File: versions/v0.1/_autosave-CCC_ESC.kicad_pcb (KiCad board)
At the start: 4 copper layers, 100 x 65 mm, 155 parts, among them J1 Conn_01x04, J2 Conn_01x04, J3 Conn_01x06, J4 Conn_01x06, U1 NCP5183, U2 NCP5183, U3 NCP5183, U4 NCS20074D, U5 STM32F401CCU6_Balckpill, U6 PQDE6W-Q110, U7 TO220_replacement_module

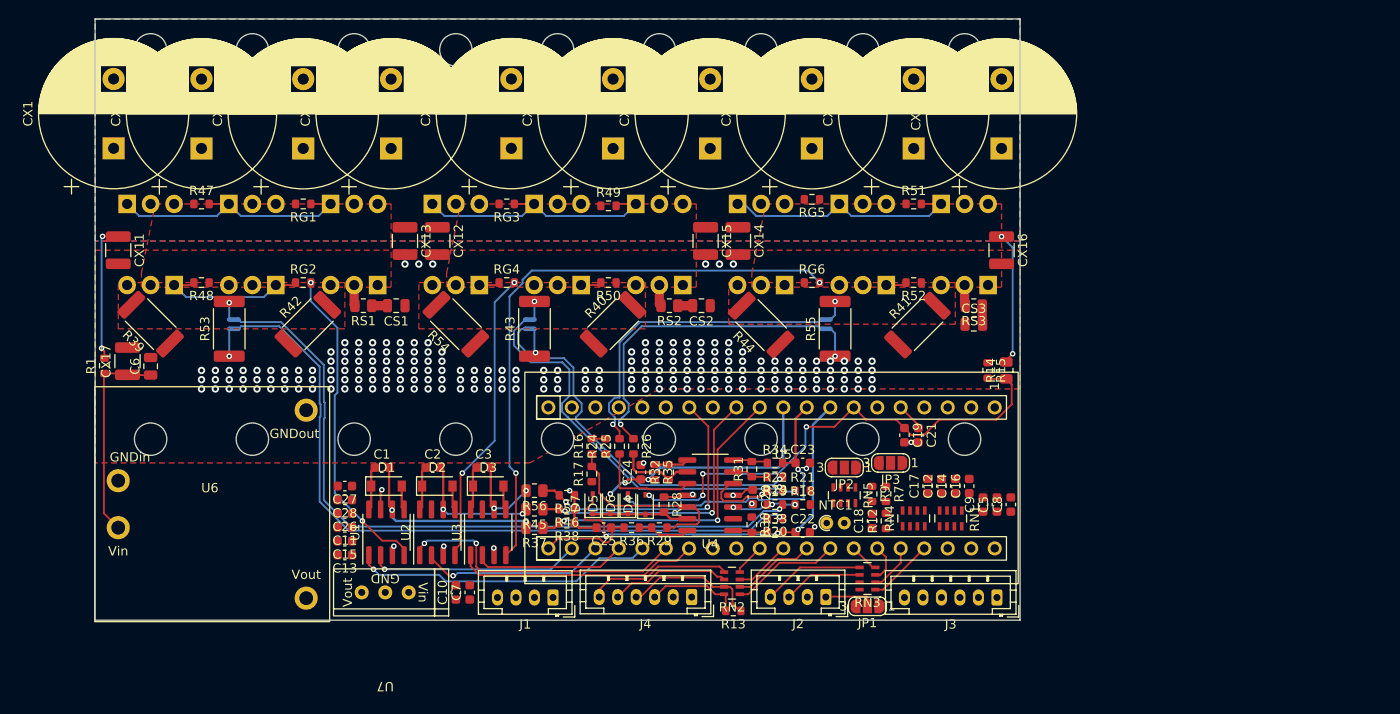
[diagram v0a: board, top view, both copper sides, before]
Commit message: work in progress - added some values and part numbers
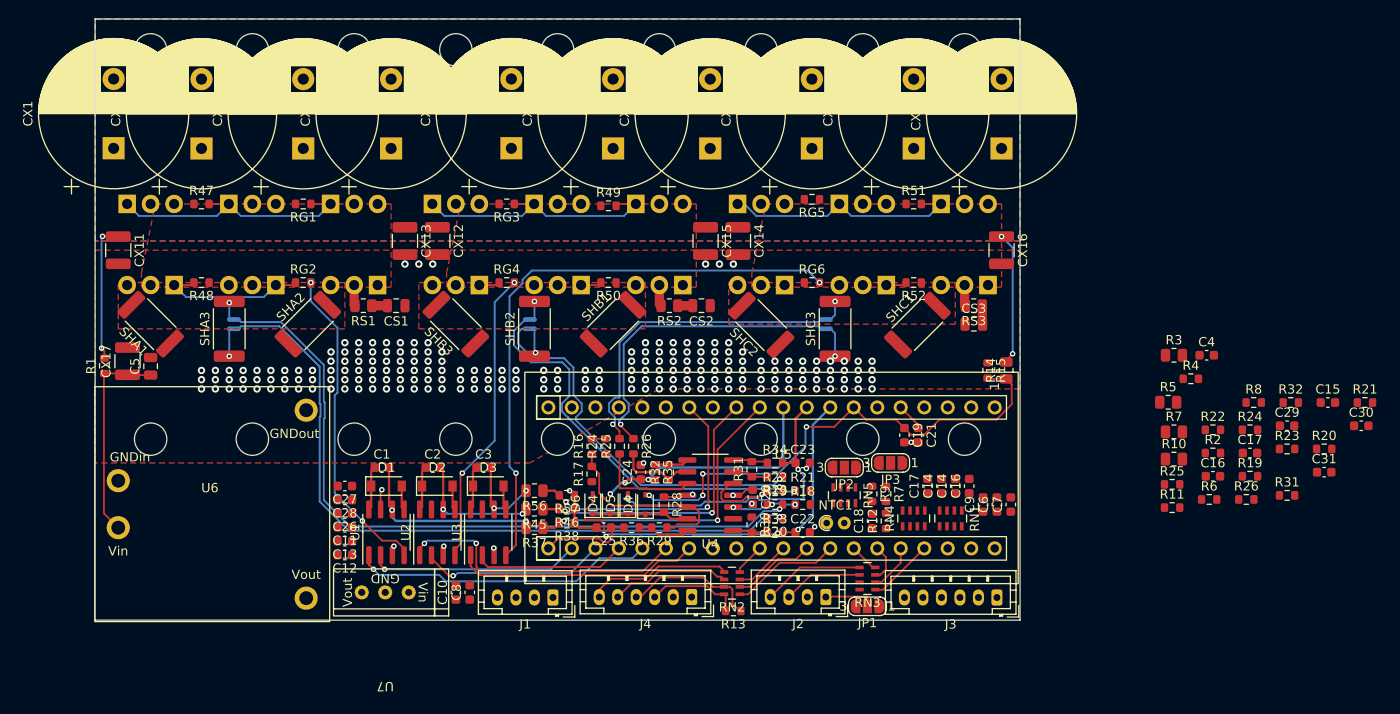
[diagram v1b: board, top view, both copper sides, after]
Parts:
- added C15: 1n5, Capacitor_SMD:C_0603_1608Metric, F.Cu at (183.3, 91.5)
- added C16: 1n5, Capacitor_SMD:C_0603_1608Metric, F.Cu at (170.8, 99.4)
- added C17: 1n5, Capacitor_SMD:C_0603_1608Metric, F.Cu at (174.9, 96.9)
- added C29: 47pF, Capacitor_SMD:C_0603_1608Metric, F.Cu at (178.9, 94.0)
- added C30: 47pF, Capacitor_SMD:C_0603_1608Metric, F.Cu at (186.9, 94.0)
- added C31: 47pF, Capacitor_SMD:C_0603_1608Metric, F.Cu at (182.9, 99.0)
- added C4: 1nF, Capacitor_SMD:C_0603_1608Metric, F.Cu at (170.2, 86.4)
- added R10: 100k, Resistor_SMD:R_0805_2012Metric, F.Cu at (166.6, 97.6)
- added R11: 3k3, Resistor_SMD:R_0603_1608Metric, F.Cu at (166.4, 102.8)
- added R19: 2k2, Resistor_SMD:R_0603_1608Metric, F.Cu at (174.9, 99.4)
- added R2: 2k2, Resistor_SMD:R_0603_1608Metric, F.Cu at (170.8, 96.9)
- added R20: 2k2, Resistor_SMD:R_0603_1608Metric, F.Cu at (182.9, 96.5)
- added R21: 47k, Resistor_SMD:R_0603_1608Metric, F.Cu at (187.3, 91.5)
- added R22: 2k2, Resistor_SMD:R_0603_1608Metric, F.Cu at (170.8, 94.4)
- added R23: 2k2, Resistor_SMD:R_0603_1608Metric, F.Cu at (178.9, 96.5)
- added R24: 47k, Resistor_SMD:R_0603_1608Metric, F.Cu at (174.9, 94.4)
- added R25: 2k2, Resistor_SMD:R_0603_1608Metric, F.Cu at (166.4, 100.3)
- added R26: 2k2, Resistor_SMD:R_0603_1608Metric, F.Cu at (174.5, 102.0)
- added R3: 1M, Resistor_SMD:R_0805_2012Metric, F.Cu at (166.6, 86.4)
- added R31: 22k, Resistor_SMD:R_0603_1608Metric, F.Cu at (178.9, 101.5)
- added R32: 22k, Resistor_SMD:R_0603_1608Metric, F.Cu at (179.3, 91.5)
- added R4: 33k, Resistor_SMD:R_0603_1608Metric, F.Cu at (168.5, 88.9)
- added R5: 100k, Resistor_SMD:R_0805_2012Metric, F.Cu at (166.0, 91.4)
- added R6: 3k3, Resistor_SMD:R_0603_1608Metric, F.Cu at (170.4, 102.0)
- added R7: 100k, Resistor_SMD:R_0805_2012Metric, F.Cu at (166.6, 94.6)
- added R8: 3k3, Resistor_SMD:R_0603_1608Metric, F.Cu at (175.3, 91.5)
- C14: renamed from C12; value 100n -> 1n5
- CX11, CX12, CX13, CX14, CX15, CX16: value 47uF -> 4.7uF
- R14: value R -> 1M
- R15: value R -> 33k
- R18: value R -> 47k
- R30: value R -> 22k
- RN1, RN4: value R_Pack04 -> 10k
- RN2, RN3: value R_Pack04 -> 100R
- RN5: value R_Pack04 -> 620R
- SHA1: renamed from R39; value R -> 1mR
- SHA2: renamed from R42; value R -> 1mR
- SHA3: renamed from R53; value R -> 1mR
- SHB1: renamed from R40; value R -> 1mR
- SHB2: renamed from R43; value R -> 1mR
- SHB3: renamed from R54; value R -> 1mR
- SHC1: renamed from R41; value R -> 1mR
- SHC2: renamed from R44; value R -> 1mR
- SHC3: renamed from R55; value R -> 1mR
- renumbered C13 to C12, C15 to C13, C6 to C5, C5 to C6, C8 to C7, C7 to C8, D5 to D4, D6 to D5, D7 to D6
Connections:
- C18 pad 1: FET_TEMP -> Net-(C18-Pad1)
- D4 pad 1: Net-(U4-Pad13) -> VSENSE2
- D5 pad 1: Net-(U4-Pad13) -> VSENSE2
- D6 pad 1: Net-(U4-Pad13) -> VSENSE2
- JP3 pad 3: Net-(U5-Pad15) -> Net-(C18-Pad1)
- R18 pad 1: Net-(U4-Pad3) -> Net-(R18-Pad1)
- R28 pad 2: Net-(U4-Pad13) -> VSENSE2
- R30 pad 1: Net-(U4-Pad2) -> Net-(R20-Pad1)
- R34 pad 1: Net-(U4-Pad7) -> Net-(R31-Pad2)
- R35 pad 1: Net-(U4-Pad8) -> Net-(R32-Pad2)
- R9 pad 1: Net-(R9-Pad1) -> GND
- R9 pad 2: GND -> Net-(R9-Pad2)
- RN5 pad 2: A_THROTTLE -> Net-(J1-Pad3)
- RN5 pad 3: Net-(J1-Pad3) -> A_THROTTLE
- RN5 pad 5: Net-(R9-Pad1) -> Net-(R9-Pad2)
- RN5 pad 6: Net-(R9-Pad1) -> Net-(RN5-Pad6)
- RN5 pad 7: Net-(R7-Pad1) -> Net-(R9-Pad2)
- RN5 pad 8: Net-(R7-Pad1) -> Net-(RN5-Pad6)
- U4 pad 10: Net-(U4-Pad10) -> Net-(R24-Pad1)
- U4 pad 13: Net-(U4-Pad13) -> VSENSE2
- U4 pad 2: Net-(U4-Pad2) -> Net-(R20-Pad1)
- U4 pad 3: Net-(U4-Pad3) -> Net-(R18-Pad1)
- U4 pad 5: Net-(U4-Pad5) -> Net-(R21-Pad1)
- U4 pad 6: Net-(U4-Pad6) -> Net-(R23-Pad1)
- U4 pad 7: Net-(U4-Pad7) -> Net-(R31-Pad2)
- U4 pad 8: Net-(U4-Pad8) -> Net-(R32-Pad2)
- U4 pad 9: Net-(U4-Pad9) -> Net-(R26-Pad1)
- U5 pad 15: Net-(U5-Pad15) -> Net-(C18-Pad1)
- U5 pad 18: unconnected-(U5-Pad18) -> V3V3
- U5 pad 28: PA11 DUSB_DM USART6_TX F412_CAN_TX -> unconnected-(U5-Pad28)
- U5 pad 29: PA12 DUSB_DP USART6_RX F412_CAN_TX -> unconnected-(U5-Pad29)
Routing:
- net VSENSE2: track 0.00 -> 10.9 mm
- net Net-(U4-Pad13): track 10.9 -> 0.00 mm
- net Net-(U4-Pad3): track 7.62 -> 0.00 mm, vias 3 -> 0
- net Net-(R18-Pad1): track 0.00 -> 7.62 mm, vias 0 -> 3
- net Net-(U4-Pad7): track 3.83 -> 0.00 mm
- net Net-(R31-Pad2): track 0.00 -> 3.83 mm
- net Net-(U4-Pad8): track 3.73 -> 0.00 mm
- net Net-(R32-Pad2): track 0.00 -> 3.73 mm
